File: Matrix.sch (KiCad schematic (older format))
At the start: 210 parts

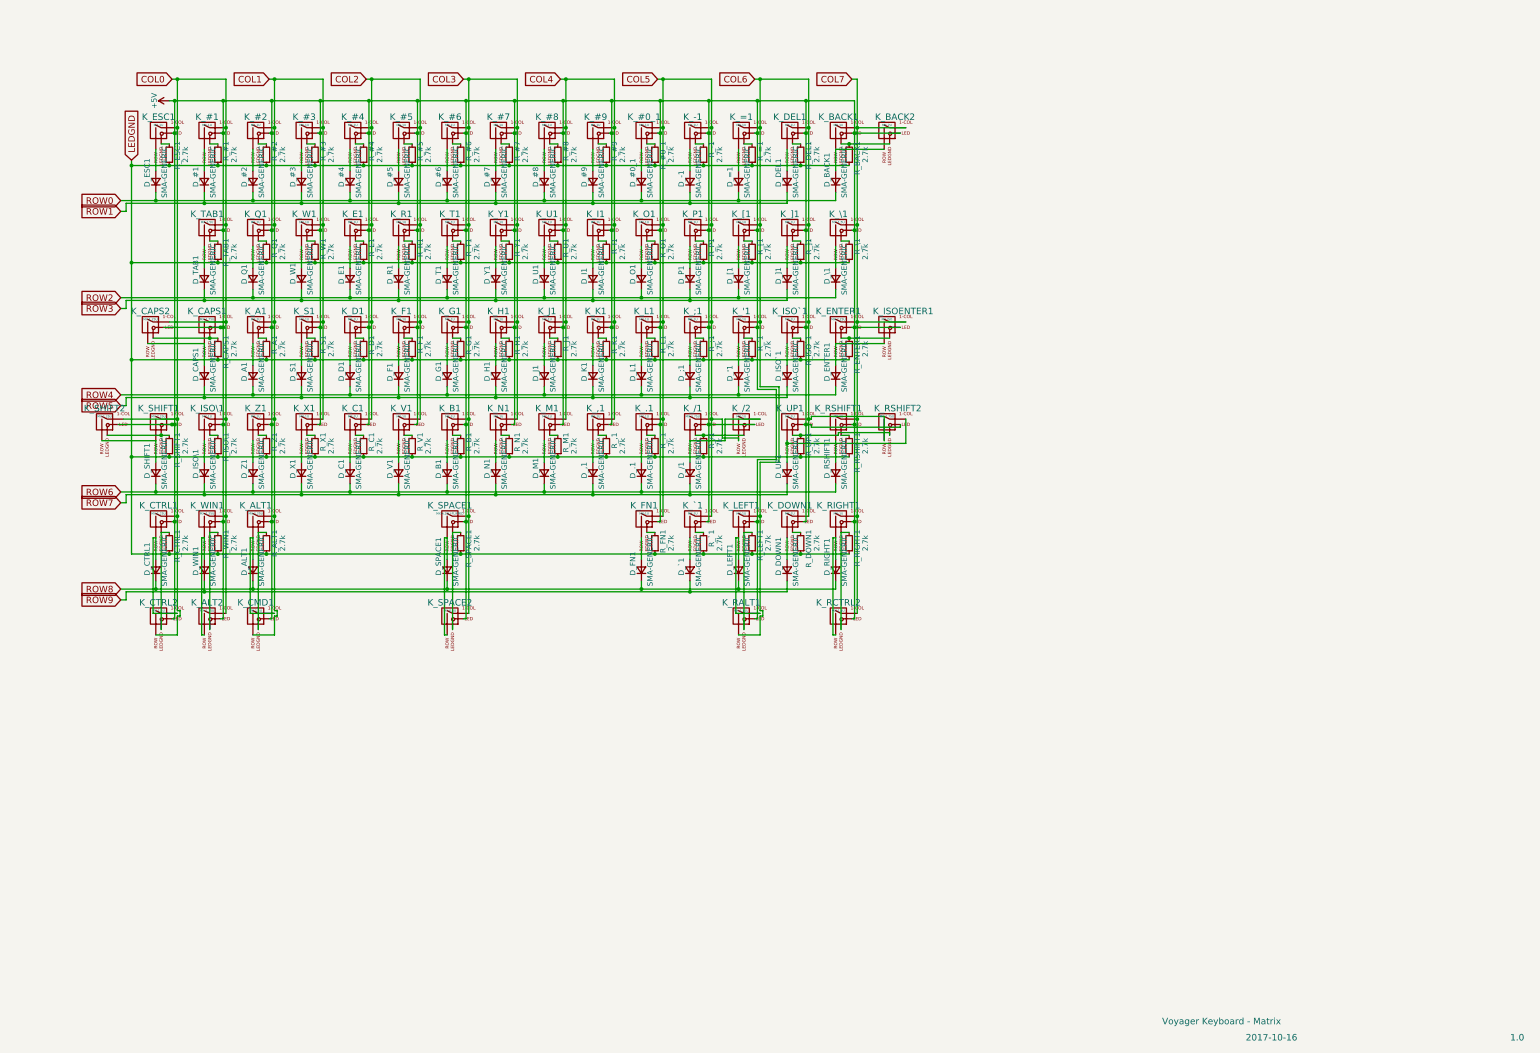
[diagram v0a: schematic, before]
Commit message: Route without MCU connections
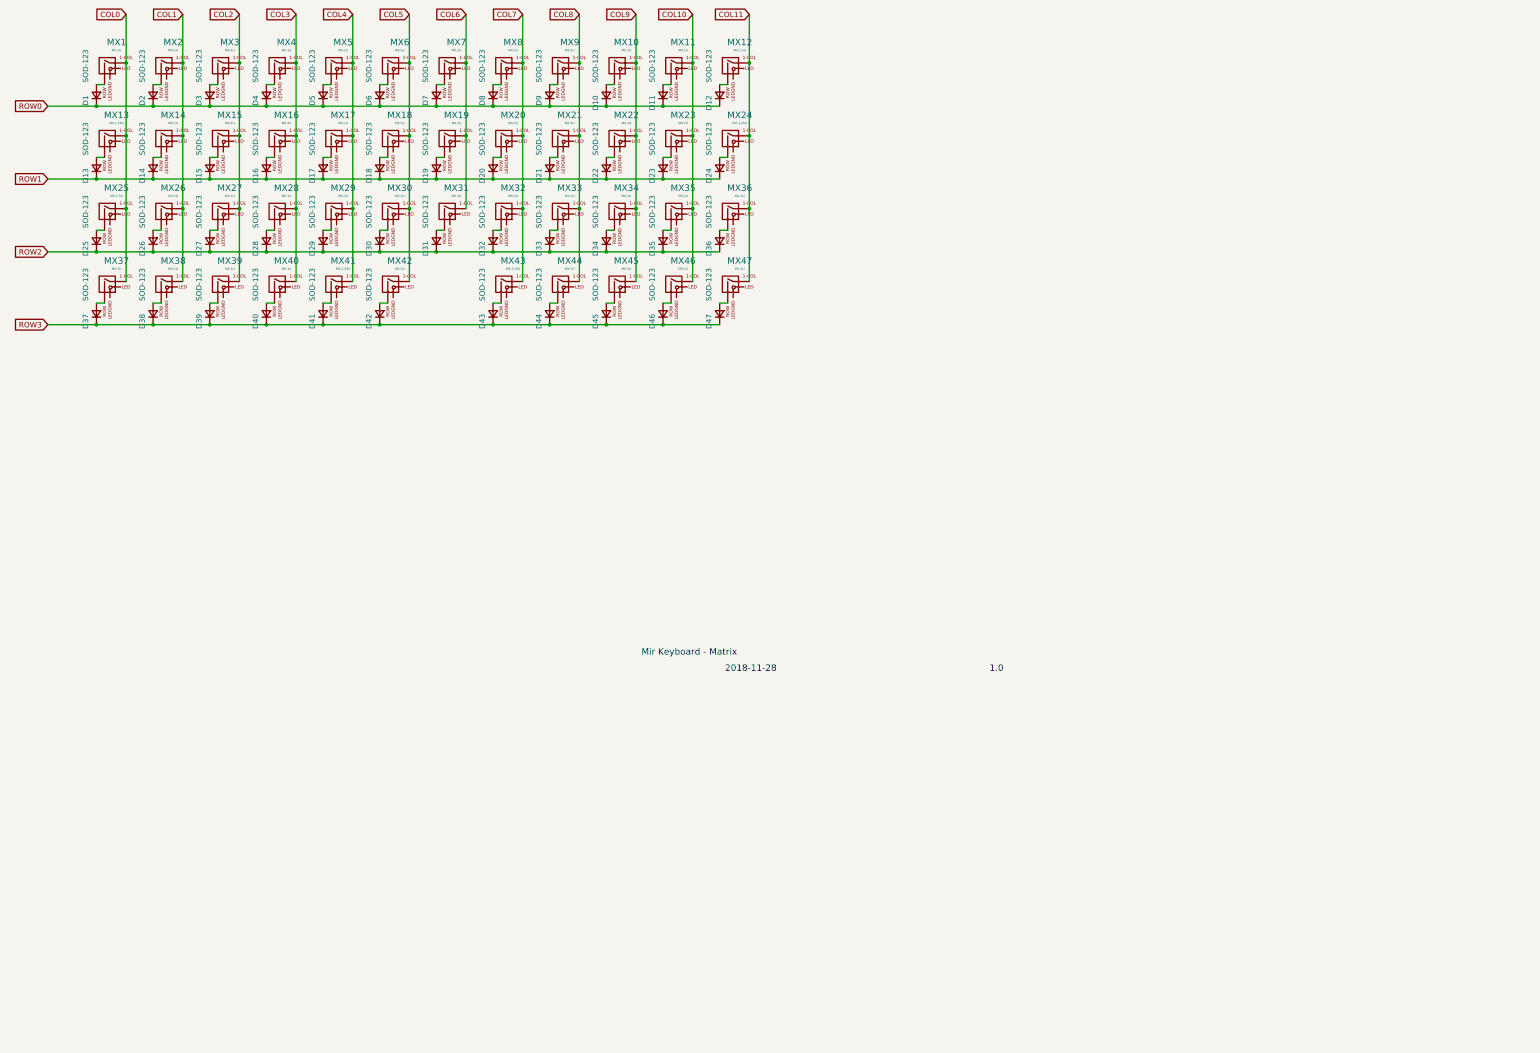
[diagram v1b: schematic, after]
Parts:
- removed D_#0_1, D_#1, D_#2, D_#3, D_#4, D_#5, D_#6, D_#7, D_#8, D_#9, D_'1, D_,1, D_-1, D_.1, D_/1, D_;1, D_=1, D_A1, D_ALT1, D_B1, D_BACK1, D_C1, D_CAPS1, D_CTRL1, D_D1, D_DEL1, D_DOWN1, D_E1, D_ENTER1, D_ESC1, D_F1, D_FN1, D_G1, D_H1, D_I1, D_ISO\1, D_ISO`1, D_J1, D_K1, D_L1, D_LEFT1, D_M1, D_N1, D_O1, D_P1, D_Q1, D_R1, D_RIGHT1, D_RSHIFT1, D_S1, D_SHIFT1, D_SPACE1, D_T1, D_TAB1, D_U1, D_UP1, D_V1, D_W1, D_WIN1, D_X1, D_Y1, D_Z1, D_[1, D_\1, D_]1, D_`1: SMA-GENERIC, Diodes_SMD:D_SOD-323_HandSoldering, symbol Device:D_Small
- removed K_#0_1, K_#1, K_#2, K_#3, K_#4, K_#5, K_#6, K_#7, K_#8, K_#9, K_'1, K_,1, K_-1, K_.1, K_/2, K_;1, K_=1, K_A1, K_B1, K_BACK1, K_C1, K_D1, K_DEL1, K_DOWN1, K_E1, K_ESC1, K_F1, K_FN1, K_G1, K_H1, K_I1, K_ISO\1, K_ISO`1, K_J1, K_K1, K_L1, K_LEFT1, K_M1, K_N1, K_O1, K_P1, K_Q1, K_R1, K_RIGHT1, K_RSHIFT1, K_S1, K_T1, K_U1, K_UP1, K_V1, K_W1, K_X1, K_Y1, K_Z1, K_[1, K_]1, K_`1: MX-1U, MX_Alps_Hybrid:MX-1U, symbol MX_Alps_Hybrids:MX-1U
- removed K_/1, K_CAPS1: MX-1.75U, MX_Alps_Hybrid:MX-1.75U, symbol MX_Alps_Hybrids:MX-1.75U
- removed K_ALT1, K_CTRL1, K_RALT1, K_SHIFT2, K_WIN1: MX-1.25U, MX_Alps_Hybrid:MX-1.25U, symbol MX_Alps_Hybrids:MX-1.25U
- removed K_ALT2, K_CAPS2: MX-1.25U, MX_Alps_Hybrid:MX-1.25U-FLIPPED, symbol MX_Alps_Hybrids:MX-1.25U-FLIPPED
- removed K_BACK2: MX-2U, MX_Alps_Hybrid:MX-2U, symbol MX_Alps_Hybrids:MX-2U
- removed K_CMD1, K_TAB1, K_\1: MX-1.5U, MX_Alps_Hybrid:MX-1.5U, symbol MX_Alps_Hybrids:MX-1.5U
- removed K_CTRL2, K_RCTRL2: MX-1.5U, MX_Alps_Hybrid:MX-1.5U-FLIPPED, symbol MX_Alps_Hybrids:MX-1.5U-FLIPPED
- removed K_ENTER1, K_SHIFT1: MX-2.25U, MX_Alps_Hybrid:MX-2.25U, symbol MX_Alps_Hybrids:MX-2.25U
- removed K_ISOENTER1: MX-ISO, MX_Alps_Hybrid:MX-ISO-Combined-ReversedStabilizers, symbol MX_Alps_Hybrids:MX-ISO
- removed K_RSHIFT2: MX-2.75U, MX_Alps_Hybrid:MX-2.75U-FLIPPED, symbol MX_Alps_Hybrids:MX-2.75U-FLIPPED
- removed K_SPACE1: MX-6.25U-FLIPPED, MX_Alps_Hybrid:MX-6.25U-ReversedStabilizers, symbol MX_Alps_Hybrids:MX-6.25U-FLIPPED
- removed K_SPACE2: MX-6.5U, MX_Alps_Hybrid:MX-6.5U, symbol MX_Alps_Hybrids:MX-6.5U
- removed R_#0_1, R_#1, R_#2, R_#3, R_#4, R_#5, R_#6, R_#7, R_#8, R_#9, R_'1, R_,1, R_-1, R_.1, R_/1, R_;1, R_=1, R_A1, R_ALT1, R_B1, R_BACK1, R_C1, R_CAPS1, R_CTRL1, R_D1, R_DEL1, R_DOWN1, R_E1, R_ENTER1, R_ESC1, R_F1, R_FN1, R_G1, R_H1, R_I1, R_ISO\1, R_ISO`1, R_J1, R_K1, R_L1, R_LEFT1, R_M1, R_N1, R_O1, R_P1, R_Q1, R_R1, R_RIGHT1, R_RSHIFT1, R_S1, R_SHIFT1, R_SPACE1, R_T1, R_TAB1, R_U1, R_UP1, R_V1, R_W1, R_WIN1, R_X1, R_Y1, R_Z1, R_[1, R_\1, R_]1, R_`1: 2.7k, Resistors_SMD:R_0805_HandSoldering, symbol Device:R_Small
- added D1, D10, D11, D12, D13, D14, D15, D16, D17, D18, D19, D2, D20, D21, D22, D23, D24, D25, D26, D27, D28, D29, D3, D30, D31, D32, D33, D34, D35, D36, D37, D38, D39, D4, D40, D41, D42, D43, D44, D45, D46, D47, D5, D6, D7, D8, D9: SOD-123, Diodes_SMD:D_SOD-123, symbol Device:D_Small
- added MX1, MX10, MX11, MX14, MX15, MX16, MX17, MX18, MX19, MX2, MX20, MX21, MX22, MX23, MX26, MX27, MX28, MX29, MX3, MX30, MX31, MX32, MX33, MX34, MX35, MX36, MX37, MX38, MX39, MX4, MX40, MX44, MX45, MX46, MX47, MX5, MX6, MX7, MX8, MX9: MX-1U, MX_Alps_Hybrid:MXOnly-1U-Hotswap, symbol MX_Alps_Hybrids:MX-1U
- added MX12, MX25: MX-1.5U, MX_Alps_Hybrid:MXOnly-1.5U-Hotswap, symbol MX_Alps_Hybrids:MX-1U
- added MX13, MX24, MX41, MX43: MX-1.25U, MX_Alps_Hybrid:MXOnly-1.25U-Hotswap, symbol MX_Alps_Hybrids:MX-1U
- added MX42: MX-2U, MX_Alps_Hybrid:MXOnly-2U-Hotswap-ReversedStabilizers, symbol MX_Alps_Hybrids:MX-1U
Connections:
- net COL0: now also MX1.1 (COL), MX13.1 (COL), MX25.1 (COL), MX37.1 (COL)
- net COL1: now also MX14.1 (COL), MX2.1 (COL), MX26.1 (COL), MX38.1 (COL)
- net COL2: now also MX15.1 (COL), MX27.1 (COL), MX3.1 (COL), MX39.1 (COL)
- net COL3: now also MX16.1 (COL), MX28.1 (COL), MX4.1 (COL), MX40.1 (COL)
- net COL4: now also MX17.1 (COL), MX29.1 (COL), MX41.1 (COL), MX5.1 (COL)
- net COL5: now also MX18.1 (COL), MX30.1 (COL), MX42.1 (COL), MX6.1 (COL)
- net COL6: now also MX19.1 (COL), MX31.1 (COL), MX7.1 (COL)
- net COL7: now also MX20.1 (COL), MX32.1 (COL), MX43.1 (COL), MX8.1 (COL)
- net ROW0: now also D1.1 (K), D10.1 (K), D11.1 (K), D12.1 (K), D2.1 (K), D3.1 (K), D4.1 (K), D5.1 (K), D6.1 (K), D7.1 (K), D8.1 (K), D9.1 (K)
- net ROW1: now also D13.1 (K), D14.1 (K), D15.1 (K), D16.1 (K), D17.1 (K), D18.1 (K), D19.1 (K), D20.1 (K), D21.1 (K), D22.1 (K), D23.1 (K), D24.1 (K)
- net ROW2: now also D25.1 (K), D26.1 (K), D27.1 (K), D28.1 (K), D29.1 (K), D30.1 (K), D31.1 (K), D32.1 (K), D33.1 (K), D34.1 (K), D35.1 (K), D36.1 (K)
- net ROW3: now also D37.1 (K), D38.1 (K), D39.1 (K), D40.1 (K), D41.1 (K), D42.1 (K), D43.1 (K), D44.1 (K), D45.1 (K), D46.1 (K), D47.1 (K)
- new net: D1.2 (A), MX1.2 (ROW)
- new net: D2.2 (A), MX2.2 (ROW)
- new net: D3.2 (A), MX3.2 (ROW)
- new net: D4.2 (A), MX4.2 (ROW)
- new net: D5.2 (A), MX5.2 (ROW)
- new net: D6.2 (A), MX6.2 (ROW)
- new net: D7.2 (A), MX7.2 (ROW)
- new net: D8.2 (A), MX8.2 (ROW)
- new net: D9.2 (A), MX9.2 (ROW)
- new net: D10.2 (A), MX10.2 (ROW)
- new net: D11.2 (A), MX11.2 (ROW)
- new net: D12.2 (A), MX12.2 (ROW)
- new net: D13.2 (A), MX13.2 (ROW)
- new net: D14.2 (A), MX14.2 (ROW)
- new net: D15.2 (A), MX15.2 (ROW)
- new net: D16.2 (A), MX16.2 (ROW)
- new net: D17.2 (A), MX17.2 (ROW)
- new net: D18.2 (A), MX18.2 (ROW)
- new net: D19.2 (A), MX19.2 (ROW)
- new net: D20.2 (A), MX20.2 (ROW)
- new net: D21.2 (A), MX21.2 (ROW)
- new net: D22.2 (A), MX22.2 (ROW)
- new net: D23.2 (A), MX23.2 (ROW)
- new net: D24.2 (A), MX24.2 (ROW)
- new net: D25.2 (A), MX25.2 (ROW)
- new net: D26.2 (A), MX26.2 (ROW)
- new net: D27.2 (A), MX27.2 (ROW)
- new net: D28.2 (A), MX28.2 (ROW)
- new net: D29.2 (A), MX29.2 (ROW)
- new net: D30.2 (A), MX30.2 (ROW)
- new net: D31.2 (A), MX31.2 (ROW)
- new net: D32.2 (A), MX32.2 (ROW)
- new net: D33.2 (A), MX33.2 (ROW)
- new net: D34.2 (A), MX34.2 (ROW)
- new net: D35.2 (A), MX35.2 (ROW)
- new net: D36.2 (A), MX36.2 (ROW)
- new net: D37.2 (A), MX37.2 (ROW)
- new net: D38.2 (A), MX38.2 (ROW)
- new net: D39.2 (A), MX39.2 (ROW)
- new net: D40.2 (A), MX40.2 (ROW)
- new net: D41.2 (A), MX41.2 (ROW)
- new net: D42.2 (A), MX42.2 (ROW)
- new net: D43.2 (A), MX43.2 (ROW)
- new net: D44.2 (A), MX44.2 (ROW)
- new net: D45.2 (A), MX45.2 (ROW)
- new net: D46.2 (A), MX46.2 (ROW)
- new net: D47.2 (A), MX47.2 (ROW)
- new net COL10: MX11.1 (COL), MX23.1 (COL), MX35.1 (COL), MX46.1 (COL)
- new net COL11: MX12.1 (COL), MX24.1 (COL), MX36.1 (COL), MX47.1 (COL)
- new net COL8: MX21.1 (COL), MX33.1 (COL), MX44.1 (COL), MX9.1 (COL)
- new net COL9: MX10.1 (COL), MX22.1 (COL), MX34.1 (COL), MX45.1 (COL)
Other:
- note added: "2018-11-28"
- note added: "Mir Keyboard - Matrix"
- note removed: "2017-10-16"
- note removed: "Voyager Keyboard - Matrix"
